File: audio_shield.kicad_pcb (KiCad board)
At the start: 2 copper layers, 11 parts, among them J1 AudioJack2, U1 LM386, U3 OPA340NA

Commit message: route the board
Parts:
- U1: footprint Package_SO:SOIC-8-1EP_3.9x4.9mm_P1.27mm_EP2.29x3mm -> Package_SO:SOIC-8_3.9x4.9mm_P1.27mm
- moved J1 80.2 mm to (168.2, 93.4), turned to 180 degrees
- moved C3 53.9 mm to (152.2, 88.9), turned to 180 degrees
- moved C2 50.2 mm to (152.3, 92.7), turned to 180 degrees
- moved C4 48.9 mm to (147.2, 93.9)
- moved R3 45.0 mm to (152.4, 96.9), turned to 180 degrees
- moved C1 38.6 mm to (137.2, 87.6), turned to 90 degrees
- moved A1 37.3 mm to (123.2, 115.5)
- moved U1 35.3 mm to (144.2, 88.4)
- moved U3 32.9 mm to (144.9, 100.0)
- moved R1 31.3 mm to (137.5, 92.7), turned to 90 degrees
- moved R2 30.9 mm to (133.9, 92.8), turned to -90 degrees
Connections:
- A1 pad 29: unconnected-(A1-GND-Pad29) -> GND
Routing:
- net GND: track 0.00 -> 158.9 mm, vias 0 -> 1
- net VCC: track 0.00 -> 28.9 mm, vias 0 -> 1
- net /LEFT_DAC: track 0.00 -> 25.0 mm
- net Net-(U3--): track 0.00 -> 11.7 mm
- net /LEFT_SPEAKER: track 0.00 -> 11.0 mm
- net Net-(C2-Pad2): track 0.00 -> 7.65 mm
- net Net-(U1-+): track 0.00 -> 5.76 mm
- net Net-(C1-Pad1): track 0.00 -> 5.50 mm
- net Net-(C2-Pad1): track 0.00 -> 4.20 mm
- added copper zone on B.Cu, net GND
- added copper zone on F.Cu, net GND
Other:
- board outline added: 53.3 x 55.9 mm

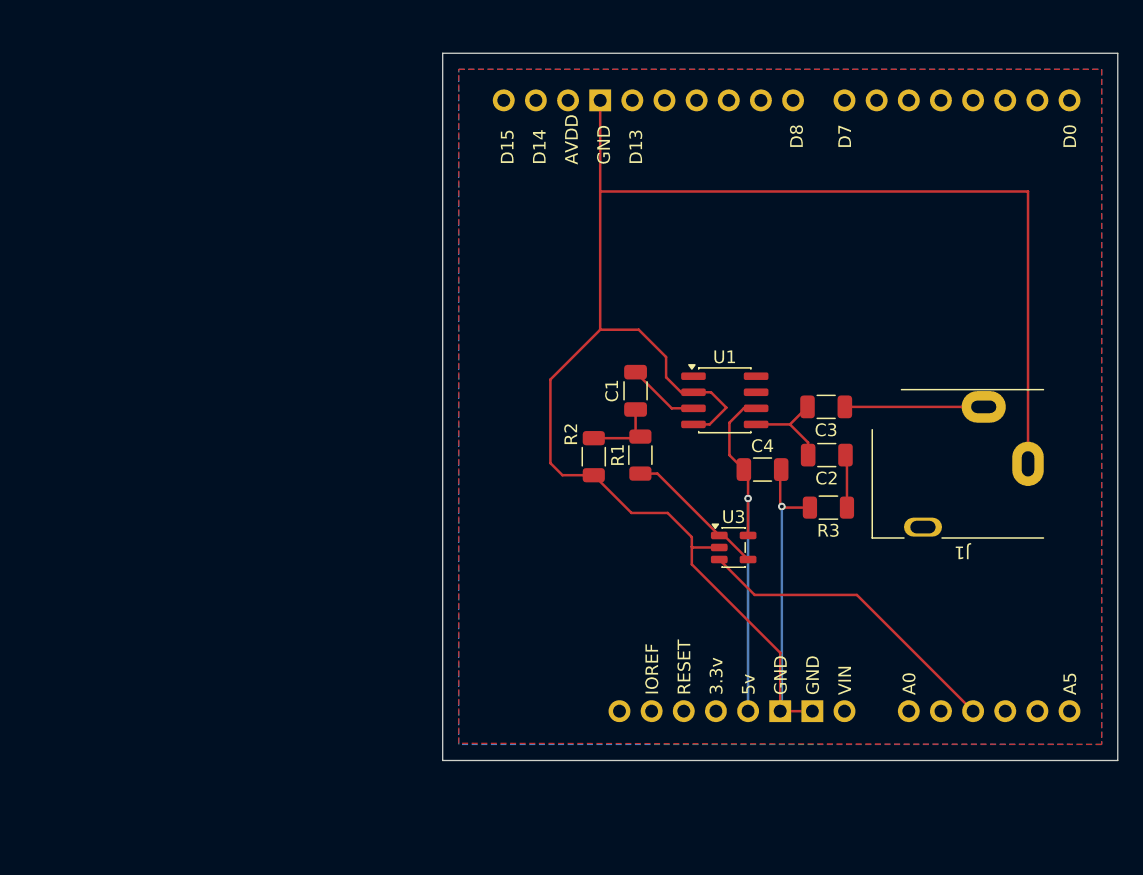
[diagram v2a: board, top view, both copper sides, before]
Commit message: just place components, rely on KiCadRoutingTools to route
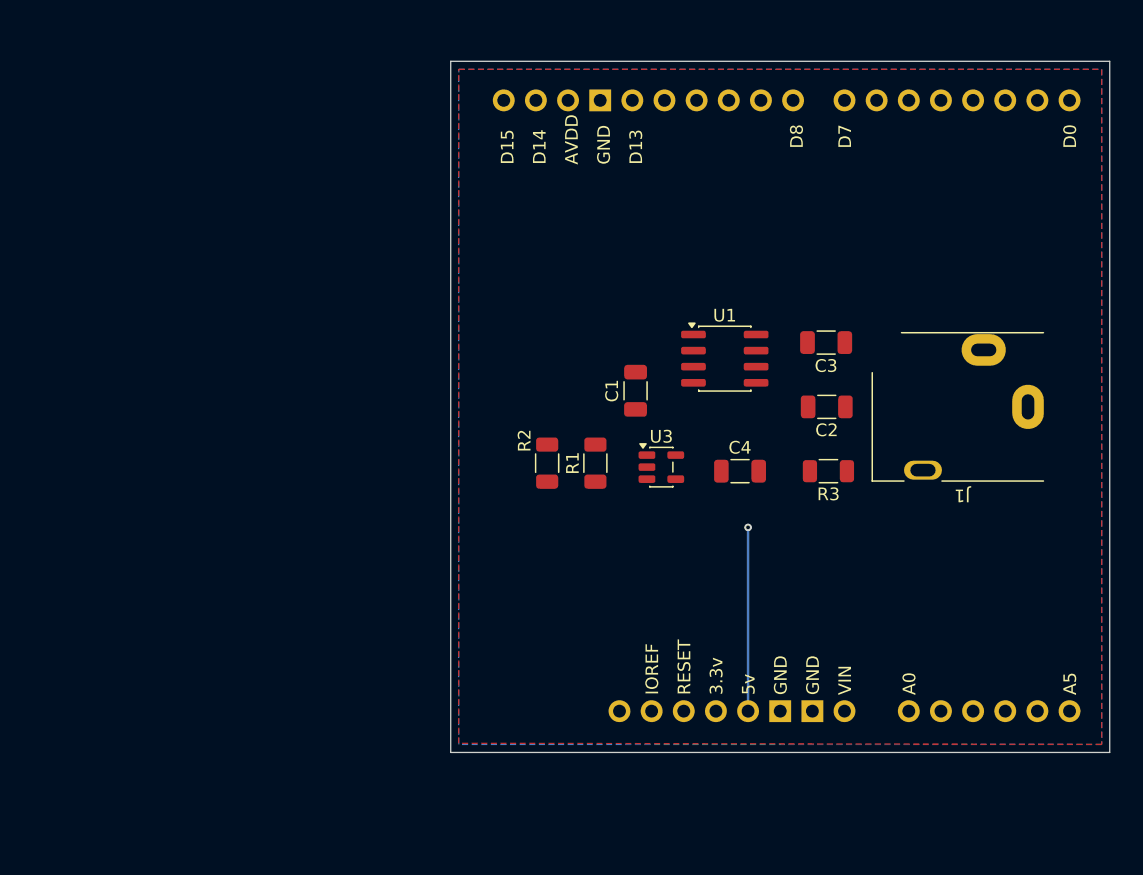
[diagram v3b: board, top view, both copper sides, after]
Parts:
- moved U3 8.54 mm to (139.2, 93.7)
- moved C3 5.08 mm to (152.2, 83.8)
- moved J1 4.50 mm to (168.2, 88.9)
- moved C2 3.81 mm to (152.3, 88.9)
- moved R2 3.72 mm to (130.2, 93.3)
- moved R1 3.61 mm to (134.0, 93.3)
- moved U1 3.29 mm to (144.2, 85.1)
- moved R3 2.88 mm to (152.4, 94.0)
- moved C4 1.78 mm to (145.4, 94.0)
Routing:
- net GND: track 158.9 -> 0.00 mm, vias 1 -> 0
- net /LEFT_DAC: track 25.0 -> 0.00 mm
- net VCC: track 28.9 -> 14.5 mm
- net Net-(U3--): track 11.7 -> 0.00 mm
- net /LEFT_SPEAKER: track 11.0 -> 0.00 mm
- net Net-(C2-Pad2): track 7.65 -> 0.00 mm
- net Net-(U1-+): track 5.76 -> 0.00 mm
- net Net-(C1-Pad1): track 5.50 -> 0.00 mm
- net Net-(C2-Pad1): track 4.20 -> 0.00 mm
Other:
- board size 53.3 x 55.9 mm -> 52.1 x 54.6 mm

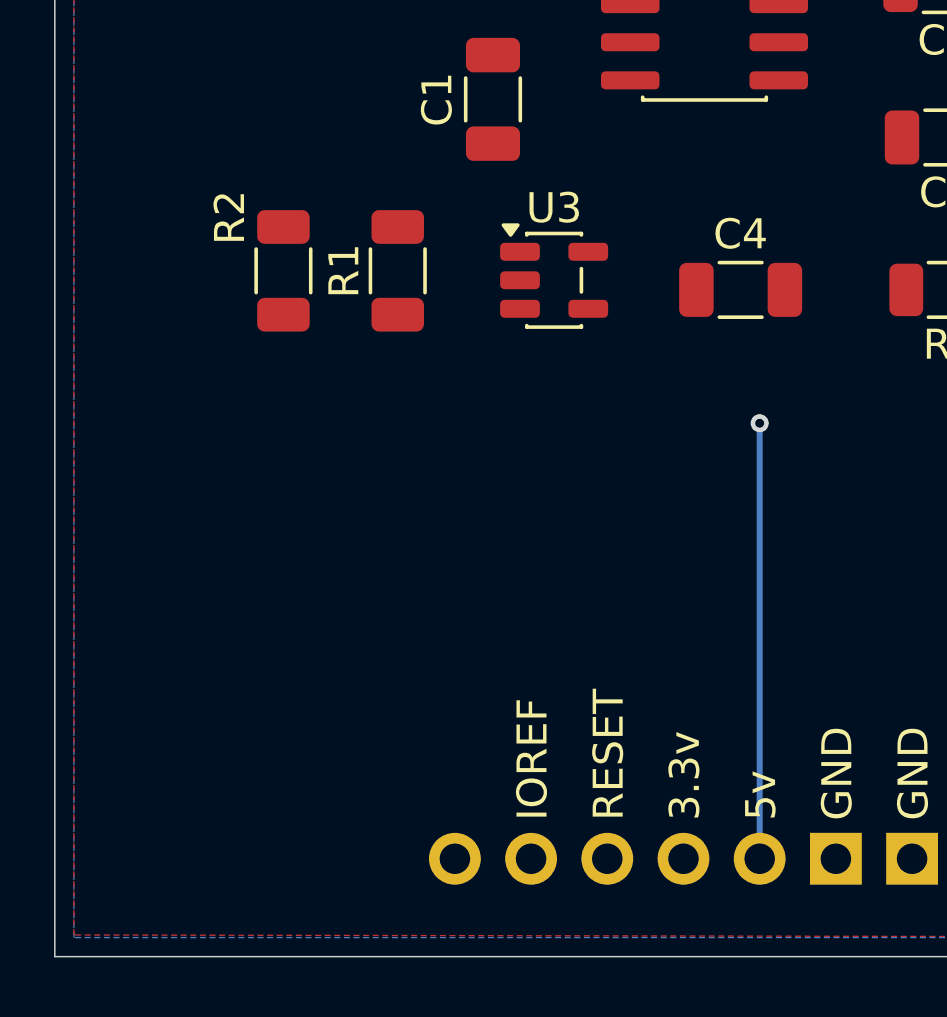
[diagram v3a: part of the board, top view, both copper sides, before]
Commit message: add power net class .5mm track thick
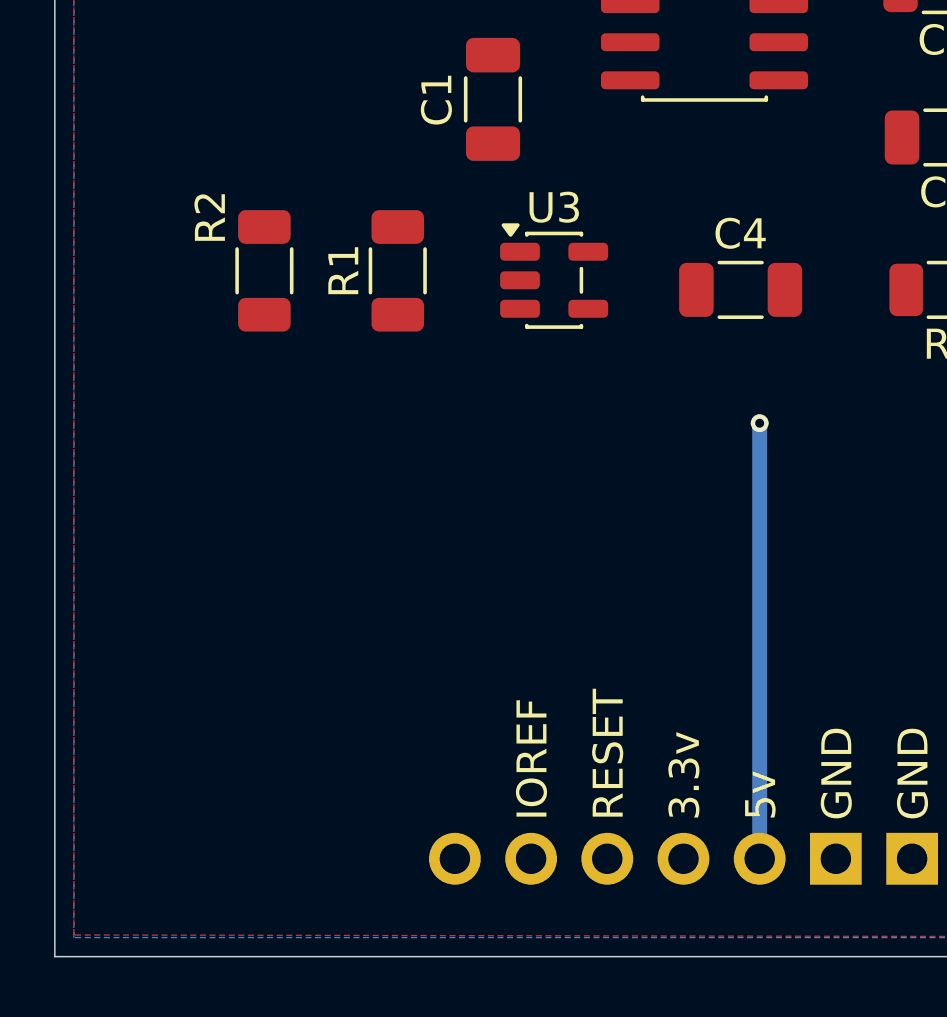
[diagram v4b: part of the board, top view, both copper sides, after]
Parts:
- moved R2 0.64 mm to (129.5, 93.3)
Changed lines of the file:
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@@
 	(footprint "Resistor_SMD:R_1206_3216Metric"
 		(layer "F.Cu")
-		(at 130.175 93.345 -90)
+		(at 129.54 93.345 -90)
 		(descr "Resistor SMD 1206 (3216 Metric), square (rectangular) end terminal, IPC-7351 nominal, (Body size source: IPC-SM-782 page 72, https://www.pcb-3d.com/wordpress/wp-content/uploads/ipc-sm-782a_amendment_1_and_2.pdf)")
 		(tags "resistor")
@@
 	)
 	(segment
-		(start 146.05 98.425)
-		(end 146.05 112.9425)
-		(width 0.2)
+		(start 146.05 112.9425)
+		(end 146.05 98.425)
+		(width 0.5)
 		(layer "B.Cu")
 		(net 9)
